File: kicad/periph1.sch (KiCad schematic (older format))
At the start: 12 parts, among them J1 SD-104031, J6 TOUCH PANEL, P1 EXPANSION, U1 IMX6UL_BGA289, U3 A7101CH

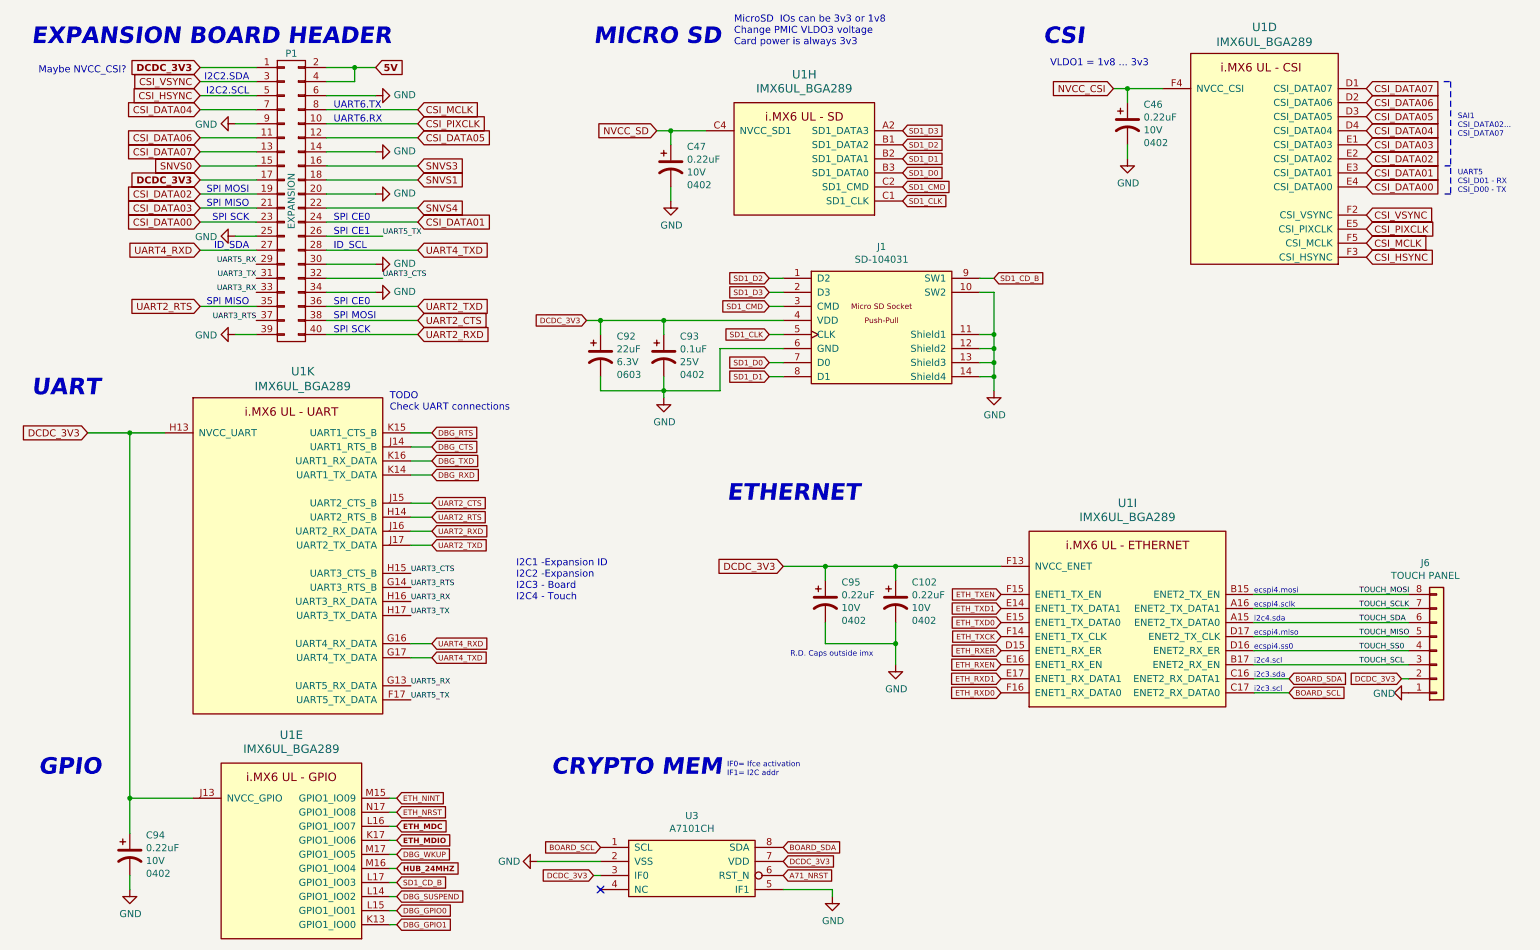
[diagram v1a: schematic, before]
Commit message: add i2c for ULZ
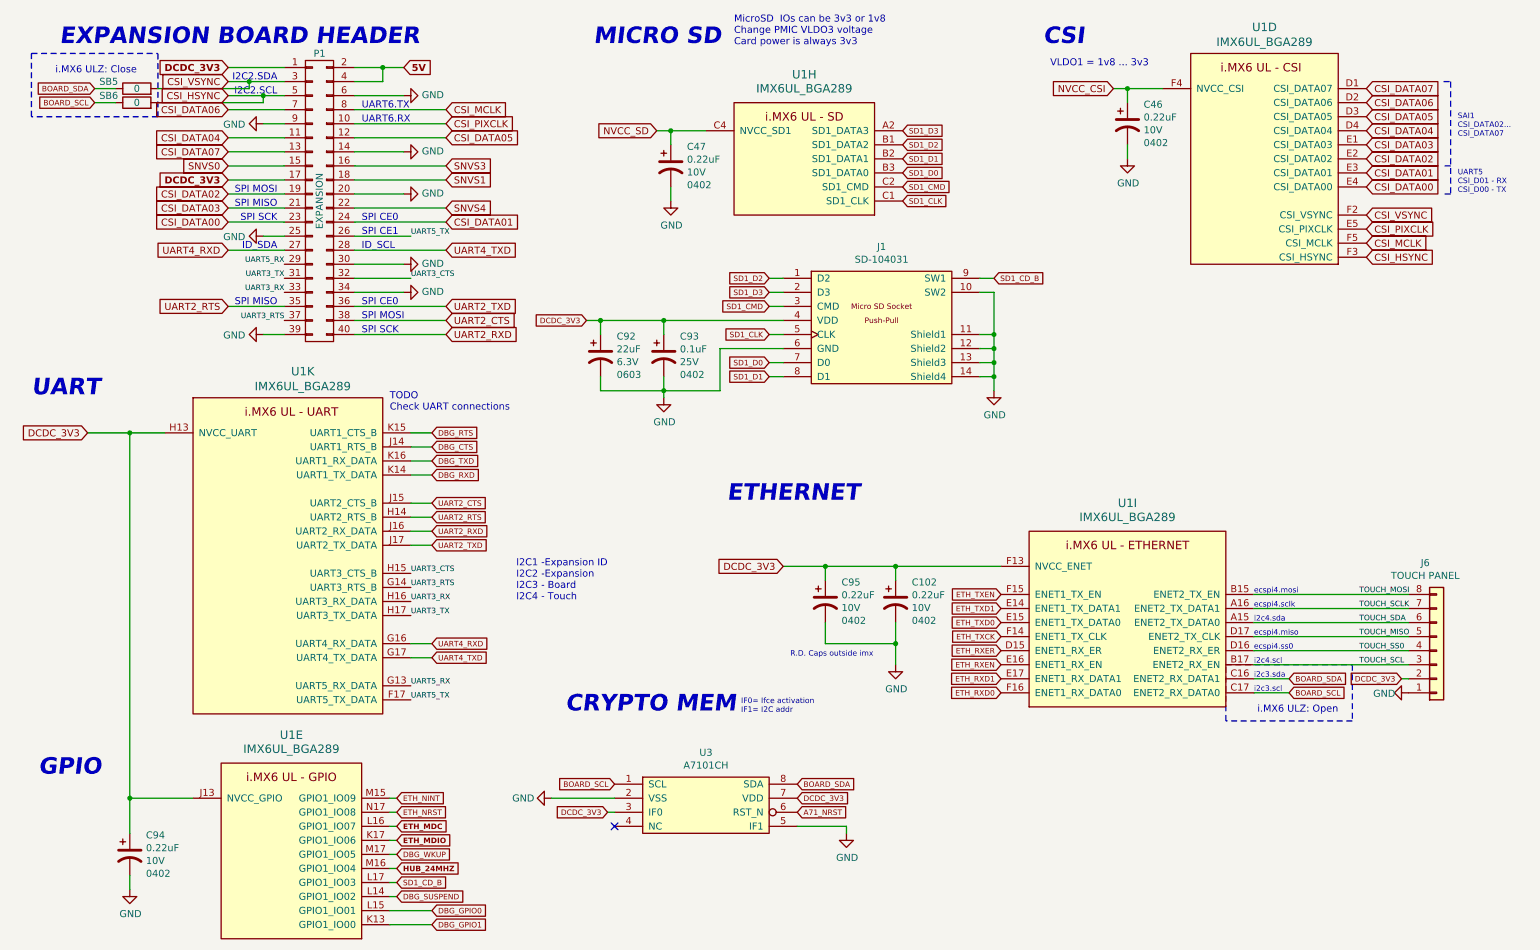
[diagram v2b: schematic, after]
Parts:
- added SB5, SB6: 0, Custom Components:R_0402_narrow, symbol nano-rescue:R
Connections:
- net BOARD_SCL: now also SB6.1
- net BOARD_SDA: now also SB5.1
- net CSI_DATA04: now also P1.11 (P11); no longer P1.7 (P7)
- net CSI_DATA06: now also P1.7 (P7); no longer P1.11 (P11)
- net CSI_HSYNC: now also SB6.2
- net CSI_VSYNC: now also SB5.2
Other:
- note added: "i.MX6 ULZ: Close"
- note added: "i.MX6 ULZ: Open"
- note removed: "Maybe NVCC_CSI?"
- moved on the sheet: P1, U3

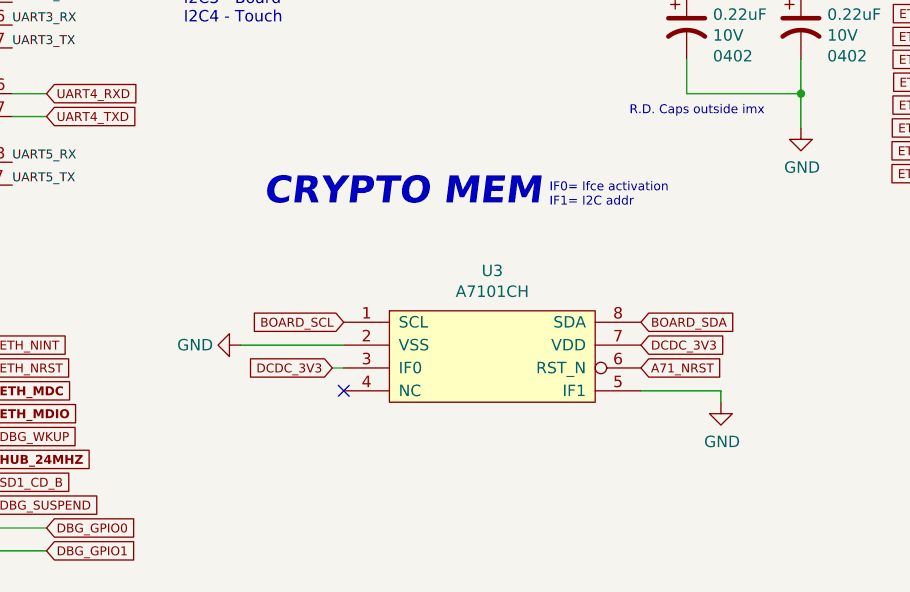
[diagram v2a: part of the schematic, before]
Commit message: pmic_int connection
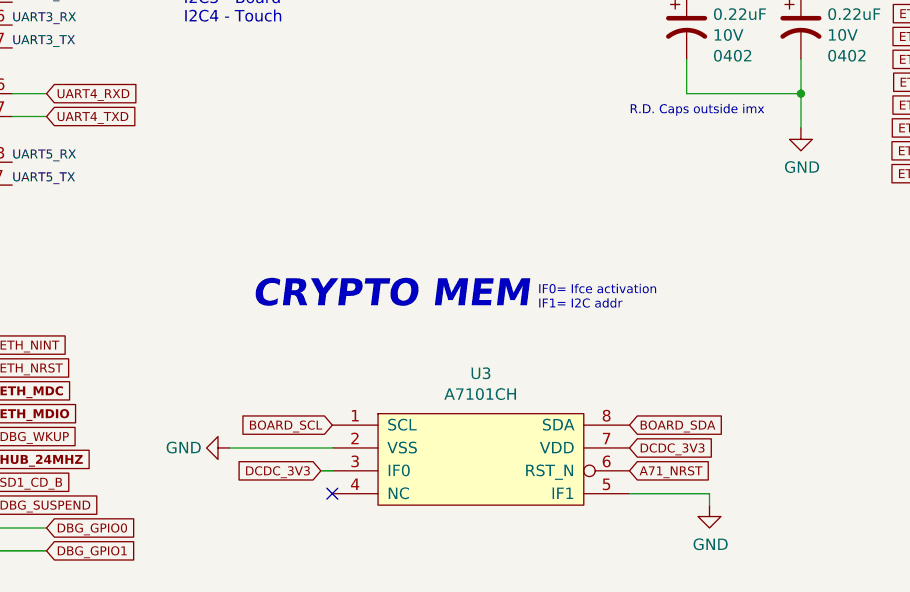
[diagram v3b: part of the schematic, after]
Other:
- moved on the sheet: U3
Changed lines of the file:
@@
 Text GLabel 3200 6350 2    39   Input ~ 8
 ETH_MDC
-Text Notes 4400 5550 0    118  Italic 24
+Text Notes 4350 6000 0    118  Italic 24
 CRYPTO MEM
 $Comp
 L custom_components:A7101CH U3
 U 1 1 5BE0FC32
-P 5400 6100
-F 0 "U3" H 5400 6375 50  0000 C CNN
-F 1 "A7101CH" H 5400 6284 50  0000 C CNN
-F 2 "Custom Components:SOT909-1" H 5400 6100 50  0001 C CNN
-F 3 "" H 5400 6100 50  0001 C CNN
-	1    5400 6100
-	1    0    0    -1
-$EndComp
-Text GLabel 6050 6150 2    39   Input ~ 0
+P 5350 6550
+F 0 "U3" H 5350 6825 50  0000 C CNN
+F 1 "A7101CH" H 5350 6734 50  0000 C CNN
+F 2 "Custom Components:SOT909-1" H 5350 6550 50  0001 C CNN
+F 3 "" H 5350 6550 50  0001 C CNN
+	1    5350 6550
+	1    0    0    -1
+$EndComp
+Text GLabel 6000 6600 2    39   Input ~ 0
 DCDC_3V3
 Wire Wire Line
@@
 Text GLabel 2000 950  0    50   Input ~ 10
 DCDC_3V3
-NoConn ~ 4750 6350
+NoConn ~ 4700 6800
 Text GLabel 5050 1400 0    50   Input ~ 0
 NVCC_SD
@@
 Text Notes 7850 950  0    50   ~ 0
 VLDO1 = 1v8 ... 3v3
-Text Notes 5650 5550 0    39   ~ 0
+Text Notes 5600 6000 0    39   ~ 0
 IF0= Ifce activation\nIF1= I2C addr
 $Comp
@@
 Text GLabel 10100 1800 2    50   Input ~ 0
 CSI_DATA00
-Text GLabel 6050 6250 2    39   Input ~ 0
+Text GLabel 6000 6700 2    39   Input ~ 0
 A71_NRST
-Text GLabel 6050 6050 2    39   Input ~ 0
+Text GLabel 6000 6500 2    39   Input ~ 0
 BOARD_SDA
-Text GLabel 4750 6050 0    39   Input ~ 0
+Text GLabel 4700 6500 0    39   Input ~ 0
 BOARD_SCL
 $Comp
 L power:GND #PWR033
 U 1 1 5C69B82C
-P 4300 6150
-F 0 "#PWR033" H 4300 5900 50  0001 C CNN
-F 1 "GND" V 4300 5950 50  0000 C CNN
-F 2 "" H 4300 6150 50  0001 C CNN
-F 3 "" H 4300 6150 50  0001 C CNN
-	1    4300 6150
+P 4250 6600
+F 0 "#PWR033" H 4250 6350 50  0001 C CNN
+F 1 "GND" V 4250 6400 50  0000 C CNN
+F 2 "" H 4250 6600 50  0001 C CNN
+F 3 "" H 4250 6600 50  0001 C CNN
+	1    4250 6600
 	0    1    1    0
 $EndComp
@@
 L power:GND #PWR034
 U 1 1 5C35172D
-P 6400 6400
-F 0 "#PWR034" H 6400 6150 50  0001 C CNN
-F 1 "GND" H 6405 6227 50  0000 C CNN
-F 2 "" H 6400 6400 50  0001 C CNN
-F 3 "" H 6400 6400 50  0001 C CNN
-	1    6400 6400
-	1    0    0    -1
-$EndComp
-Wire Wire Line
-	6400 6350 6400 6400
-Wire Wire Line
-	6050 6350 6400 6350
-Wire Wire Line
-	4300 6150 4750 6150
-Text GLabel 4700 6250 0    39   Input ~ 0
+P 6350 6850
+F 0 "#PWR034" H 6350 6600 50  0001 C CNN
+F 1 "GND" H 6355 6677 50  0000 C CNN
+F 2 "" H 6350 6850 50  0001 C CNN
+F 3 "" H 6350 6850 50  0001 C CNN
+	1    6350 6850
+	1    0    0    -1
+$EndComp
+Wire Wire Line
+	6350 6800 6350 6850
+Wire Wire Line
+	6000 6800 6350 6800
+Wire Wire Line
+	4250 6600 4700 6600
+Text GLabel 4650 6700 0    39   Input ~ 0
 DCDC_3V3
 Wire Wire Line
-	4700 6250 4750 6250
+	4650 6700 4700 6700
 Wire Wire Line
 	9300 4700 10400 4700
